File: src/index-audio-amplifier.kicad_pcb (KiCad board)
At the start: 2 copper layers, 0 parts

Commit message: Create board edge, 0.5mm clearance from nominal
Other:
- board outline added: 23.5 x 23.5 mm
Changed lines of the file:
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@@
 		(allow_soldermask_bridges_in_footprints no)
 		(tenting front back)
+		(grid_origin 148.5 105)
 		(pcbplotparams
 			(layerselection 0x00000000_00000000_55555555_5755f5ff)
@@
 		(layer "Cmts.User")
 	)
+	(gr_circle
+		(center 148.5 105)
+		(end 160.25 105)
+		(stroke
+			(width 0.5)
+			(type solid)
+		)
+		(fill no)
+		(layer "Edge.Cuts")
+	)
 	(embedded_fonts no)

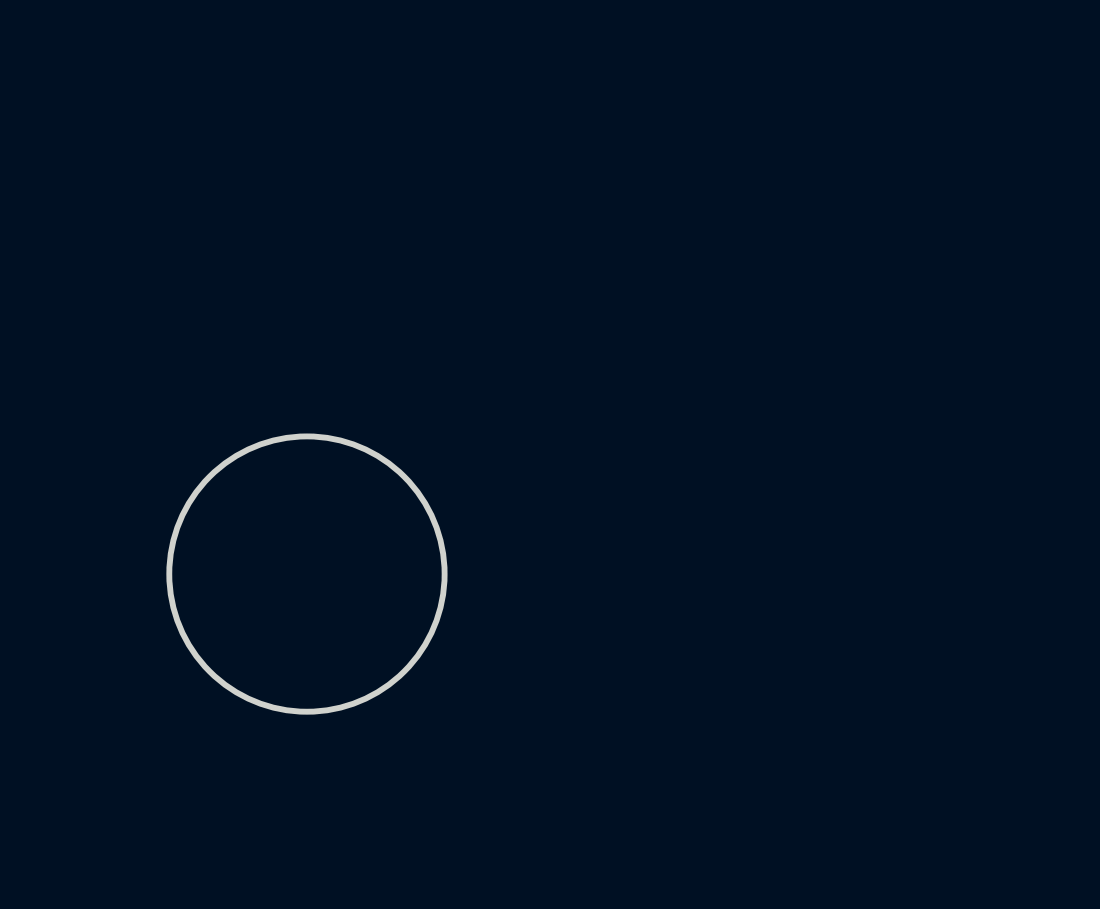
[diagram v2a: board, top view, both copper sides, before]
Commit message: Initial layout of primarily analogue section
Removed screwhead keepout in the process; I figure we'll have a high
enough standoff to avoid any shorts, as we need all the real estate we
can get!
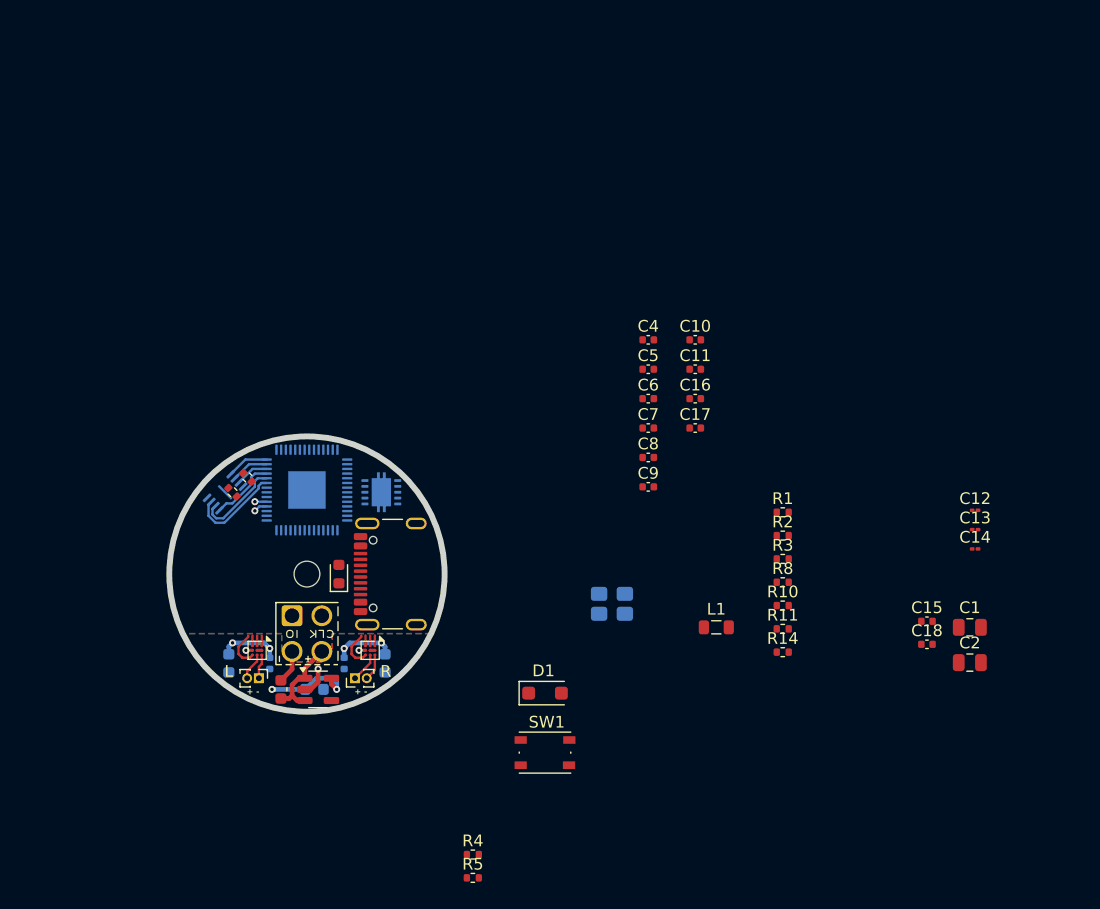
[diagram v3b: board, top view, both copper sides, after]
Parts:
- added C1: 47u, Capacitor_SMD:C_0805_2012Metric, F.Cu at (205.1, 109.5)
- added C10: 100n, Capacitor_SMD:C_0402_1005Metric, F.Cu at (181.6, 85.0)
- added C101: 1u, Capacitor_SMD:C_0603_1608Metric, F.Cu at (146.3, 114.8)
- added C102: 1u, Capacitor_SMD:C_0603_1608Metric, B.Cu at (149.1, 114.8)
- added C11: 100n, Capacitor_SMD:C_0402_1005Metric, F.Cu at (181.6, 87.5)
- added C12: 2u2, Capacitor_SMD:C_01005_0402Metric, F.Cu at (205.5, 99.6)
- added C13: 2u2, Capacitor_SMD:C_01005_0402Metric, F.Cu at (205.5, 101.2)
- added C14: 2u2, Capacitor_SMD:C_01005_0402Metric, F.Cu at (205.5, 102.9)
- added C15: 100n, Capacitor_SMD:C_0402_1005Metric, F.Cu at (201.4, 109.0)
- added C16: 15p, Capacitor_SMD:C_0402_1005Metric, F.Cu at (181.6, 90.0)
- added C17: 15p, Capacitor_SMD:C_0402_1005Metric, F.Cu at (181.6, 92.5)
- added C18: 2u2, Capacitor_SMD:C_0402_1005Metric, F.Cu at (201.4, 111.0)
- added C19: 10u, Capacitor_SMD:C_0603_1608Metric, B.Cu at (155.2, 112.6)
- added C2: 47u, Capacitor_SMD:C_0805_2012Metric, F.Cu at (205.1, 112.6)
- added C20: 100n, Capacitor_SMD:C_0402_1005Metric, B.Cu at (151.7, 112.6)
- added C21: 10u, Capacitor_SMD:C_0603_1608Metric, B.Cu at (141.8, 112.6)
- added C22: 100n, Capacitor_SMD:C_0402_1005Metric, B.Cu at (145.3, 112.6)
- added C4: 100n, Capacitor_SMD:C_0402_1005Metric, F.Cu at (177.6, 85.0)
- added C5: 100n, Capacitor_SMD:C_0402_1005Metric, F.Cu at (177.6, 87.5)
- added C6: 100n, Capacitor_SMD:C_0402_1005Metric, F.Cu at (177.6, 90.0)
- added C7: 100n, Capacitor_SMD:C_0402_1005Metric, F.Cu at (177.6, 92.5)
- added C8: 100n, Capacitor_SMD:C_0402_1005Metric, F.Cu at (177.6, 95.0)
- added C9: 100n, Capacitor_SMD:C_0402_1005Metric, F.Cu at (177.6, 97.6)
- added D1: MBR120VLSFT1G, Diode_SMD:D_SOD-123F, F.Cu at (168.8, 115.2)
- added D2: Green, LED_SMD:LED_0603_1608Metric, F.Cu at (151.2, 105.0)
- added H1: MountingHole, MountingHole:MountingHole_2.2mm_M2_ISO7380, F.Cu at (148.5, 105.0)
- added J1: USB_C_Receptacle_USB2.0_16P, Connector_USB:USB_C_Receptacle_GCT_USB4105-xx-A_16P_TopMnt_Horizontal, F.Cu at (156.8, 105.0)
- added J2: SWD_PicoprobeCandybar, Connector_PicoprobeCandybar:SWD_PicoprobeCandybar_PressFit_Compact, F.Cu at (148.5, 112.6)
- added J3: Conn_01x02, Connector_PinHeader_1.00mm:PinHeader_1x02_P1.00mm_Vertical, F.Cu at (152.6, 113.9)
- added J4: Conn_01x02, Connector_PinHeader_1.00mm:PinHeader_1x02_P1.00mm_Vertical, F.Cu at (144.4, 113.9)
- added L1: 2u2, Inductor_SMD:L_0805_2012Metric, F.Cu at (183.4, 109.5)
- added R1: 10K, Resistor_SMD:R_0402_1005Metric, F.Cu at (189.1, 99.7)
- added R10: 5K6, Resistor_SMD:R_0402_1005Metric, F.Cu at (189.1, 107.7)
- added R11: 1K, Resistor_SMD:R_0402_1005Metric, F.Cu at (189.1, 109.7)
- added R12: 27R, Resistor_SMD:R_0402_1005Metric, F.Cu at (143.4, 96.7)
- added R13: 27R, Resistor_SMD:R_0402_1005Metric, F.Cu at (142.2, 98.0)
- added R14: 1K, Resistor_SMD:R_0402_1005Metric, F.Cu at (189.1, 111.7)
- added R2: 100K, Resistor_SMD:R_0402_1005Metric, F.Cu at (189.1, 101.7)
- added R3: 470R, Resistor_SMD:R_0402_1005Metric, F.Cu at (189.1, 103.7)
- added R4: 5K11, Resistor_SMD:R_0402_1005Metric, F.Cu at (162.7, 128.9)
- added R5: 5K11, Resistor_SMD:R_0402_1005Metric, F.Cu at (162.7, 130.9)
- added R8: 100K, Resistor_SMD:R_0402_1005Metric, F.Cu at (189.1, 105.7)
- added SW1: SW_Push, Button_Switch_SMD:SW_Push_1P1T_NO_Vertical_Wuerth_434133025816, F.Cu at (168.8, 120.2)
- added U1: RP2040, Package_DFN_QFN:QFN-56-1EP_7x7mm_P0.4mm_EP3.2x3.2mm, B.Cu at (148.5, 97.8)
- added U2: RT6150B-33GQW, Package_SON:Texas_DRC0010J, B.Cu at (154.8, 98.0)
- added U3: W25Q16JVUXIQ, Package_SON:Winbond_USON-8-1EP_3x2mm_P0.5mm_EP0.2x1.6mm, B.Cu at (141.5, 98.0)
- added U4: MAX98360CENL, ProjectFootprints_IndexAudioAmplifier:WLP-9_1.347x1.347mm_Layout3x3_P0.4mm, F.Cu at (144.2, 111.5)
- added U5: TLV70033_SOT23-5, Package_TO_SOT_SMD:SOT-23-5, F.Cu at (149.5, 114.8)
- added U6: MAX98360CENL, ProjectFootprints_IndexAudioAmplifier:WLP-9_1.347x1.347mm_Layout3x3_P0.4mm, F.Cu at (153.9, 111.5)
- added X1: 12MHz, Crystal:Crystal_SMD_3225-4Pin_3.2x2.5mm, B.Cu at (174.5, 107.5)
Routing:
- net +3V3A: track 0.00 -> 19.1 mm, vias 0 -> 6
- net Net-(U1-QSPI_SD3): track 0.00 -> 8.02 mm
- net VSYS: track 0.00 -> 7.44 mm
- net Net-(U1-QSPI_SCLK): track 0.00 -> 7.27 mm
- net Net-(U1-QSPI_SD0): track 0.00 -> 5.68 mm
- net Net-(U1-GPIO17): track 0.00 -> 4.22 mm
- net Net-(U1-GPIO16): track 0.00 -> 4.22 mm
- net AGND: track 0.00 -> 3.62 mm, vias 0 -> 3
- net Net-(U1-QSPI_SS): track 0.00 -> 3.59 mm
- net Net-(U1-QSPI_SD1): track 0.00 -> 3.22 mm
- net GND: track 0.00 -> 2.87 mm
- net Net-(U1-QSPI_SD2): track 0.00 -> 2.84 mm
- net /RIGHT_P: track 0.00 -> 2.52 mm
- net /LEFT_N: track 0.00 -> 2.44 mm
- net /LEFT_P: track 0.00 -> 2.33 mm
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- added copper zone on F.Cu, net +3V3A
- added copper zone on B.Cu, net AGND
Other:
- board text added: "+ -"
- board text added: "L"
- board text added: "R"

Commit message: Consider adding USB hub controller, second port
Still a major work-in-progress;
Going to revise heavily after this commit.
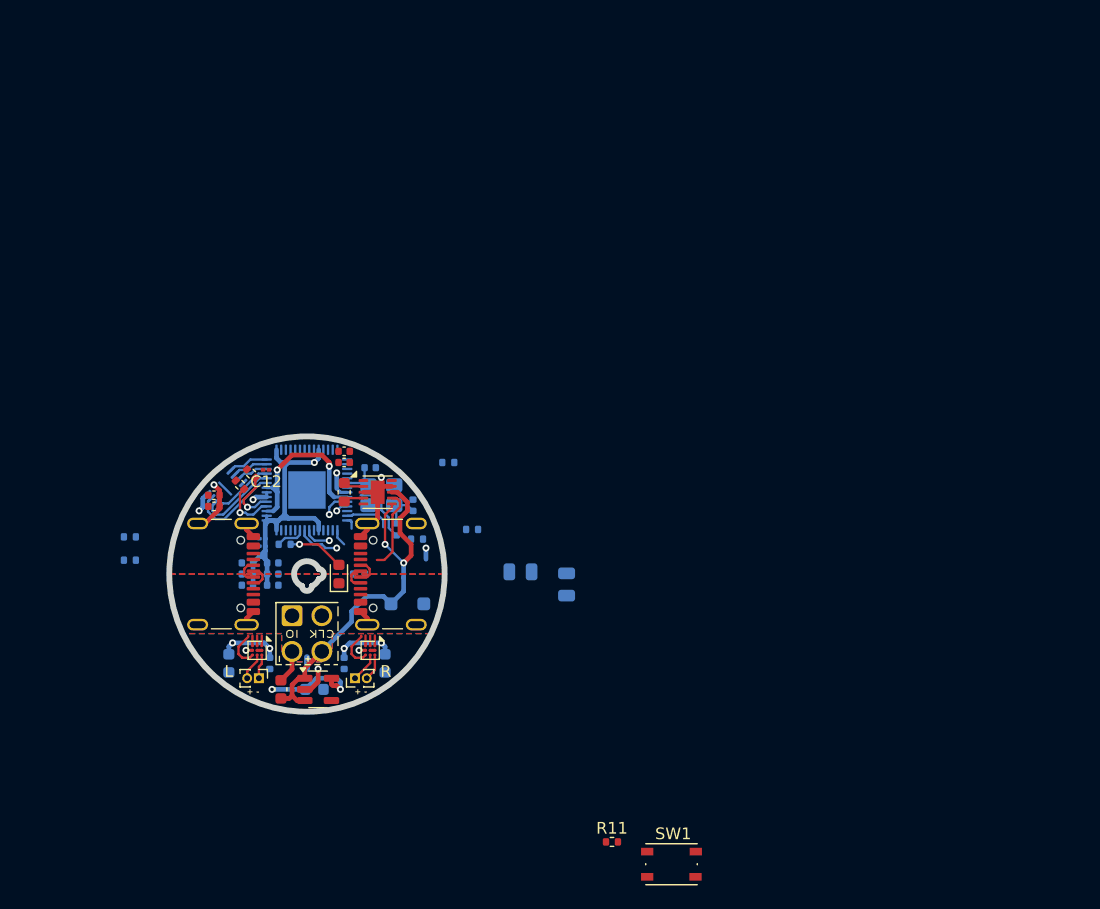
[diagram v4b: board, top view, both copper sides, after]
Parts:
- removed H1: MountingHole, MountingHole:MountingHole_2.2mm_M2_ISO7380
- added J5: USB_C_Receptacle_USB2.0_16P, Connector_USB:USB_C_Receptacle_GCT_USB4105-xx-A_16P_TopMnt_Horizontal, F.Cu at (140.2, 105.0)
- added NT1: NetTie_2, NetTie:NetTie-2_SMD_Pad0.5mm, B.Cu at (148.5, 112.6)
- C1, C10, C13, C14, C16, C17, C2, C4, C5, C6, C7, C8, D1, R1, R10, R14, R2, R3, R4, R5, R8: moved to B.Cu
- L1: footprint Inductor_SMD:L_0805_2012Metric -> Inductor_SMD:L_0603_1608Metric
- U2: footprint Package_SON:Texas_DRC0010J -> Package_SON:WSON-10-1EP_2.5x2.5mm_P0.5mm_EP1.2x2mm; moved to F.Cu
- moved C18 62.0 mm to (140.6, 99.2)
- moved C15 61.8 mm to (140.6, 98.3)
- moved C13 60.9 mm to (144.7, 102.6), turned to 180 degrees
- moved C14 60.8 mm to (144.7, 102.0), turned to 180 degrees
- moved C12 60.6 mm to (145.0, 96.1), turned to 180 degrees
- moved R3 42.5 mm to (146.6, 102.5)
- moved C10 41.7 mm to (145.6, 106.0)
- moved R5 41.3 mm to (133.4, 101.8)
- moved C4 40.1 mm to (143.4, 106.0), turned to 180 degrees
- moved C1 38.6 mm to (166.7, 104.8), turned to 180 degrees
- moved R4 38.6 mm to (133.4, 103.8)
- moved C5 38.4 mm to (143.4, 105.0), turned to 180 degrees
- moved C6 37.0 mm to (143.4, 104.0), turned to 180 degrees
- moved R10 36.3 mm to (152.9, 105.0), turned to 180 degrees
- moved C2 35.1 mm to (170.7, 105.9), turned to -90 degrees
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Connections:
- R10 pad 1: Net-(D1-A) -> VSYS
- R12 pad 1: Net-(J1-D+-PadA6) -> Net-(U1-USB_DP)
- R12 pad 2: Net-(U1-USB_DP) -> unconnected-(R12-Pad2)
- R13 pad 1: Net-(J1-D--PadA7) -> Net-(U1-USB_DM)
- R13 pad 2: Net-(U1-USB_DM) -> unconnected-(R13-Pad2)
- U2 pad 6: /3V3_EN -> VSYS
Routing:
- net +3V3: track 0.00 -> 35.5 mm, vias 0 -> 5
- net VSYS: track 7.44 -> 33.7 mm, vias 0 -> 2
- net GND: track 2.87 -> 20.3 mm, vias 0 -> 2
- net +1V1: track 0.00 -> 15.2 mm, vias 0 -> 2
- net /GPIO23: track 0.00 -> 9.32 mm, vias 0 -> 1
- net Net-(U1-XOUT): track 0.00 -> 5.54 mm
- net Net-(D2-A): track 0.00 -> 4.85 mm, vias 0 -> 1
- net Net-(U1-GPIO16): track 4.22 -> 8.13 mm
- net Net-(U1-USB_DP): track 1.01 -> 4.87 mm
- net /GPIO24: track 0.00 -> 3.65 mm, vias 0 -> 1
- net Net-(U1-USB_DM): track 1.16 -> 4.80 mm
- net Net-(U1-XIN): track 0.00 -> 3.53 mm
- net Net-(C17-Pad1): track 0.00 -> 3.43 mm
- net Net-(U1-GPIO25): track 0.00 -> 2.54 mm
- net Net-(J2-SWCLK): track 0.00 -> 2.36 mm, vias 0 -> 1
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- added copper zone on F.Cu, net +3V3
- added copper zone on B.Cu, net GND
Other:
- outline, holes or cut-outs redrawn

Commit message: Begin design refactor w/ dual stack USB-C port...
Gonna keep changing dramatically as I settle in on a design approach,
but wanted to save some layout here as a "checkpoint" to possibly refer
back to.
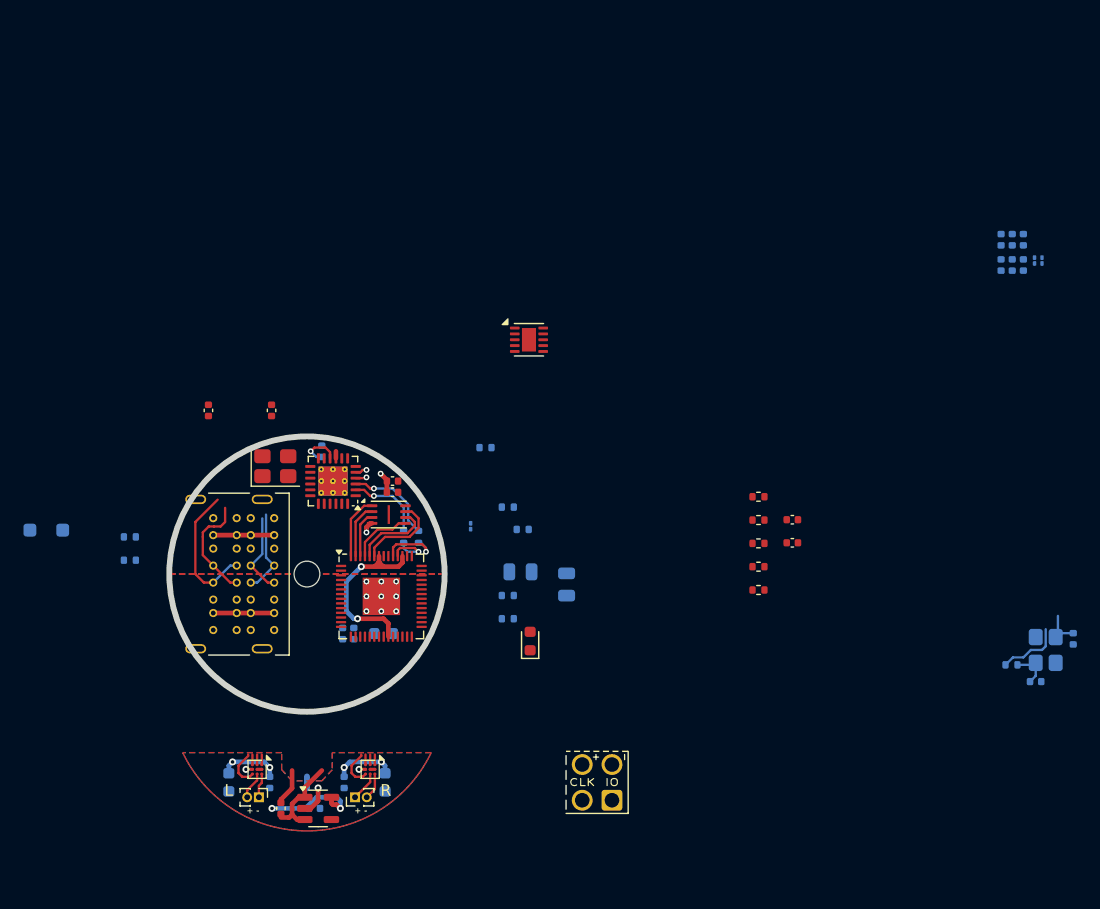
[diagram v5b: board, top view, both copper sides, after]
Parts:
- removed J5: USB_C_Receptacle_USB2.0_16P, Connector_USB:USB_C_Receptacle_GCT_USB4105-xx-A_16P_TopMnt_Horizontal
- removed R11: 1K, Resistor_SMD:R_0402_1005Metric
- removed SW1: SW_Push, Button_Switch_SMD:SW_Push_1P1T_NO_Vertical_Wuerth_434133025816
- added C23: 1u, Capacitor_SMD:C_0402_1005Metric, F.Cu at (189.9, 100.4)
- added C24: 100n, Capacitor_SMD:C_0402_1005Metric, F.Cu at (189.9, 102.3)
- added C25: 18p, Capacitor_SMD:C_0402_1005Metric, F.Cu at (140.1, 91.0)
- added C26: 18p, Capacitor_SMD:C_0402_1005Metric, F.Cu at (145.5, 91.0)
- added C3: 1u, Capacitor_SMD:C_0402_1005Metric, B.Cu at (149.8, 94.5)
- added H1: MountingHole, MountingHole:MountingHole_2.2mm_M2_ISO7380, B.Cu at (148.5, 105.0)
- added R15: 50K, Resistor_SMD:R_0402_1005Metric, F.Cu at (187.0, 104.4)
- added R17: 50K, Resistor_SMD:R_0402_1005Metric, F.Cu at (187.0, 106.4)
- added R6: 100K, Resistor_SMD:R_0402_1005Metric, F.Cu at (187.0, 98.4)
- added R7: 56K, Resistor_SMD:R_0402_1005Metric, F.Cu at (187.0, 100.4)
- added R9: 56K, Resistor_SMD:R_0402_1005Metric, F.Cu at (187.0, 102.4)
- added U7: USB2422, Package_DFN_QFN:VQFN-24-1EP_4x4mm_P0.5mm_EP2.5x2.5mm_ThermalVias, F.Cu at (150.7, 97.1)
- added X2: 24MHz, Crystal:Crystal_SMD_3225-4Pin_3.2x2.5mm, F.Cu at (145.8, 95.8)
- C101, C102: footprint Capacitor_SMD:C_0603_1608Metric -> Capacitor_SMD:C_0402_1005Metric
- C11, C12, C9, L1, R12, R13: moved to B.Cu
- J1: value USB_C_Receptacle_USB2.0_16P -> CU3616SASCLA004-LF; footprint Connector_USB:USB_C_Receptacle_GCT_USB4105-xx-A_16P_TopMnt_Horizontal -> ProjectFootprints_IndexAudioAmplifier:USB_C_Receptacle_CviLux_CU36SASCLA004-LF
- R1: value 10K -> 12K
- R10: value 5K6 -> 50K
- U1, U3: moved to F.Cu
- moved C6 71.7 mm to (209.7, 76.5), turned to 90 degrees
- moved C5 71.2 mm to (208.7, 76.5), turned to 90 degrees
- moved C4 70.8 mm to (207.7, 76.5), turned to 90 degrees
- moved C14 70.7 mm to (211.2, 78.2), turned to -90 degrees
- moved C13 70.3 mm to (210.6, 78.2), turned to -90 degrees
- moved C7 68.9 mm to (209.7, 78.6), turned to -90 degrees
- moved C8 68.4 mm to (208.7, 78.6), turned to -90 degrees
- moved C10 67.9 mm to (207.7, 78.6), turned to -90 degrees
- moved C16 61.8 mm to (213.9, 110.5), turned to -90 degrees
- moved X1 58.2 mm to (211.6, 111.5), turned to -90 degrees
- moved C17 55.2 mm to (210.7, 114.2), turned to 0 degrees
- moved R14 53.8 mm to (208.6, 112.7), turned to 180 degrees
- moved D1 31.5 mm to (126.2, 101.2)
- moved J2 25.9 mm to (173.3, 120.2), turned to 180 degrees
- moved R3 20.1 mm to (165.6, 108.8)
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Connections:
- net Net-(U1-GPIO15) renamed /AMP_EN
- net Net-(U1-GPIO16) renamed /AMP_BCLK
- net Net-(U1-GPIO17) renamed /AMP_FCLK
- net Net-(U1-GPIO18) renamed /AMP_DATA
- D1 pad 2: Net-(D1-A) -> VBUS
- R1 pad 1: /GPIO24 -> GND
- R1 pad 2: GND -> Net-(U7-RBIAS)
- R10 pad 1: VSYS -> +3V3
- R10 pad 2: /GPIO24 -> /HUB_SUSP
- R12 pad 1: Net-(U1-USB_DP) -> /RP2_DP
- R12 pad 2: unconnected-(R12-Pad2) -> Net-(U1-USB_DP)
- R13 pad 1: Net-(U1-USB_DM) -> /RP2_DM
- R13 pad 2: unconnected-(R13-Pad2) -> Net-(U1-USB_DM)
- R2 pad 1: VSYS -> VBUS
- R2 pad 2: /3V3_EN -> Net-(U7-VBUS_DET)
- R4 pad 1: Net-(J1-CC2) -> Net-(J1A-CC2_LO)
- R5 pad 1: Net-(J1-CC1) -> Net-(J1A-CC1_LO)
- U1 pad 36: /GPIO24 -> unconnected-(U1-GPIO24-Pad36)
- U1 pad 38: unconnected-(U1-GPIO26_ADC0-Pad38) -> /HUB_SUSP
- U1 pad 39: unconnected-(U1-GPIO27_ADC1-Pad39) -> /HUB_RST
- U1 pad 40: unconnected-(U1-GPIO28_ADC2-Pad40) -> /HUB_SMCK
- U1 pad 41: unconnected-(U1-GPIO29_ADC3-Pad41) -> /HUB_SMDT
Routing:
- net +3V3: track 35.5 -> 0.60 mm, vias 5 -> 0
- net VSYS: track 33.7 -> 7.44 mm, vias 2 -> 0
- net /DM_IN: track 0.00 -> 11.6 mm
- net GND: track 20.3 -> 9.44 mm, vias 2 -> 11
- net VBUS: track 0.00 -> 10.4 mm
- net /GPIO23: track 9.32 -> 0.00 mm, vias 1 -> 0
- net /DP_IN: track 0.00 -> 9.28 mm
- net /RP2_DP: track 0.00 -> 7.84 mm, vias 0 -> 1
- net /RP2_DM: track 0.00 -> 6.73 mm, vias 0 -> 1
- net /AUX_DM: track 2.25 -> 8.19 mm, vias 0 -> 1
- net /AUX_DP: track 2.19 -> 8.05 mm, vias 0 -> 1
- net Net-(D2-A): track 4.85 -> 0.00 mm, vias 1 -> 0
- net /AMP_BCLK: track 8.13 -> 4.22 mm
- net /GPIO24: track 3.65 -> 0.00 mm, vias 1 -> 0
- net Net-(U7-CRFILT): track 0.00 -> 3.63 mm, vias 0 -> 1
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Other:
- outline, holes or cut-outs redrawn
